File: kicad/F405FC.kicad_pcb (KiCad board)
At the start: 4 copper layers, 36 x 36 mm, 154 parts, among them J1 USB4105-GF-A, J2 ESC, J3 HD VTX, J4 GPS, J5 ELRS, P1 VBAT, P10 LED_DIN, P11 5V, P13 5V, P14 BUZ_N, P15 UART5_TX, P16 UART5_RX, P17 UART6_TX, P18 UART6_RX, P19 MOTOR5, P2 GND, P20 MOTOR6, P21 MOTOR7, P22 MOTOR8, P23 RSSI_IN, P24 GND, P25 5V, P3 10V, P4 GND, P5 CAM1_VID, P6 CAM2_VID, P7 VTX_VID, P8 5V, P9 GND, Q1 PMV40UN2, Q2 NX7002AK, SW1 BOOT, U1 LMR38020FSDDAR, U10 W25N01GV, U11 TS5A3159A, U12 SN74LV1T125, U13 USBLC6-2SC6, U2 LMR38020FSDDAR, U3 STM32F405RGT6, U4 LP38692MP-3.3, U5 LP5907MFX-3.3, U6 ICM-42688-P, U7 BMI270, U8 BMP390, U9 IIS2MDC, Y1 8MHz

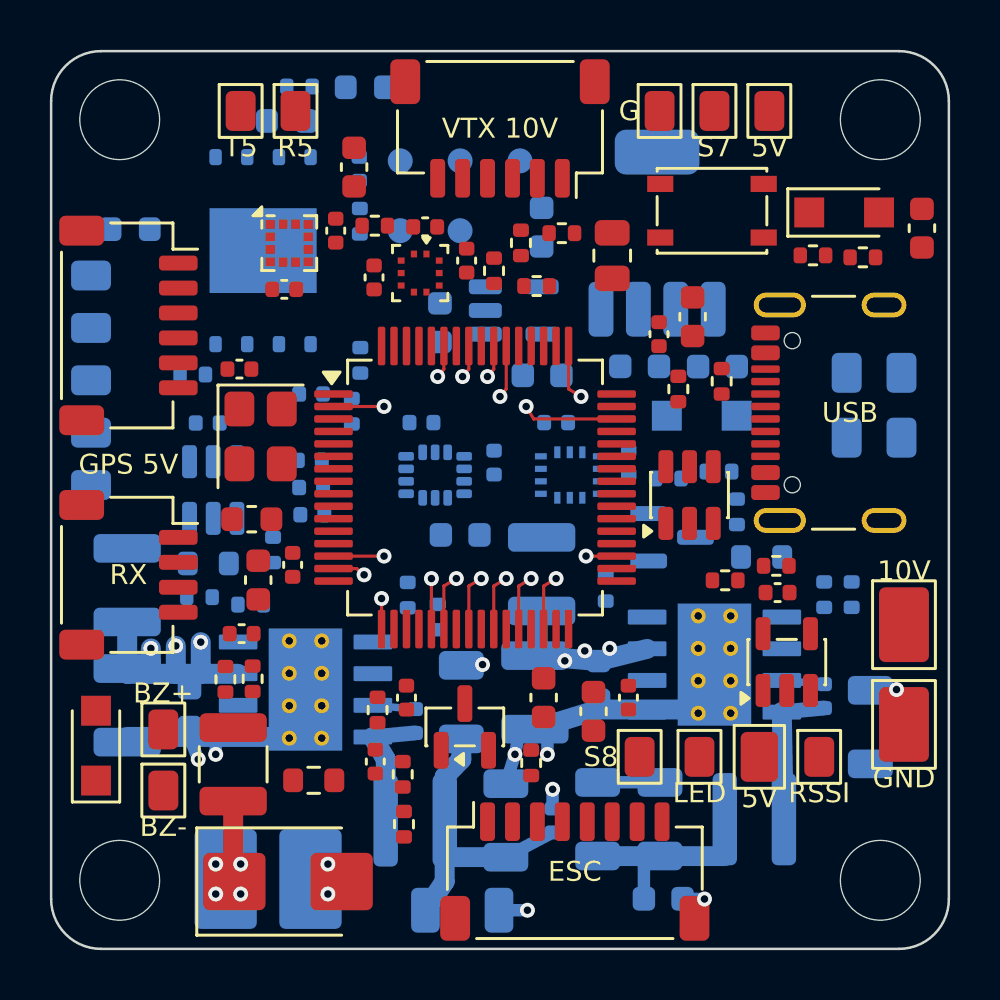
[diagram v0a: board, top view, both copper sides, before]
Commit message: Freerouting finishing step (gen/fr_finish.sh, route.py lockall stage)
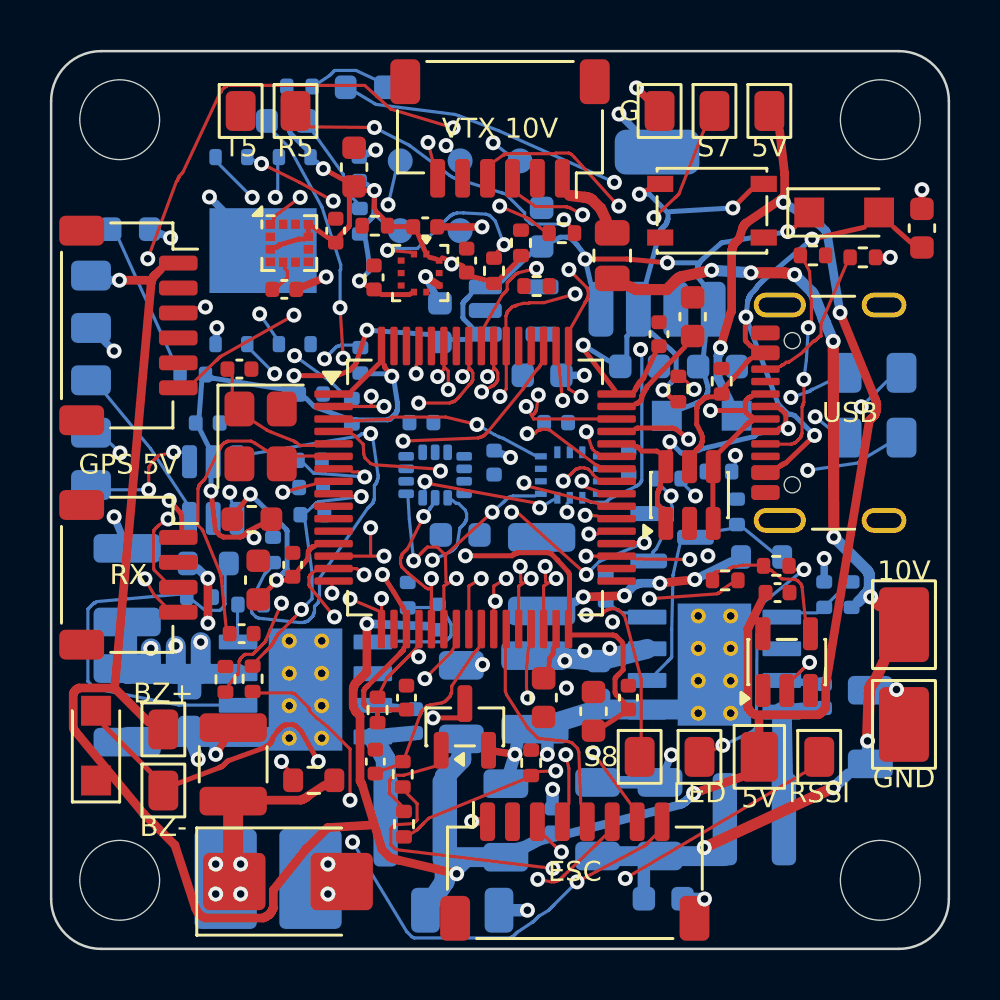
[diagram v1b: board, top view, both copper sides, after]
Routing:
- net 5V: track 10.5 -> 121.7 mm, vias 0 -> 7
- net 3V3: track 0.00 -> 90.8 mm, vias 0 -> 13
- net NRST: track 0.00 -> 38.0 mm, vias 0 -> 4
- net 5V_SYS: track 0.00 -> 33.7 mm, vias 0 -> 6
- net 10V: track 6.81 -> 38.8 mm, vias 0 -> 9
- net STATUS_LED_BLUE: track 1.22 -> 32.3 mm, vias 1 -> 3
- net GND: track 24.6 -> 53.4 mm, vias 11 -> 28
- net ESC_TLM: track 1.32 -> 29.3 mm, vias 1 -> 4
- net I2C1_SCL: track 0.00 -> 27.1 mm, vias 0 -> 5
- net VTX_PWR_EN: track 0.00 -> 26.2 mm, vias 0 -> 3
- net STATUS_LED_GREEN: track 0.00 -> 26.0 mm, vias 0 -> 5
- net SPI3_MISO: track 0.00 -> 23.2 mm, vias 0 -> 2
- net RSSI_IN: track 0.00 -> 21.0 mm, vias 0 -> 2
- net VBUS: track 0.00 -> 20.4 mm, vias 0 -> 3
- net CAM_SEL: track 2.03 -> 21.7 mm, vias 1 -> 3
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
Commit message: Freerouting finish in progress: base route set from PathFinder (6 conflicting nets dropped)
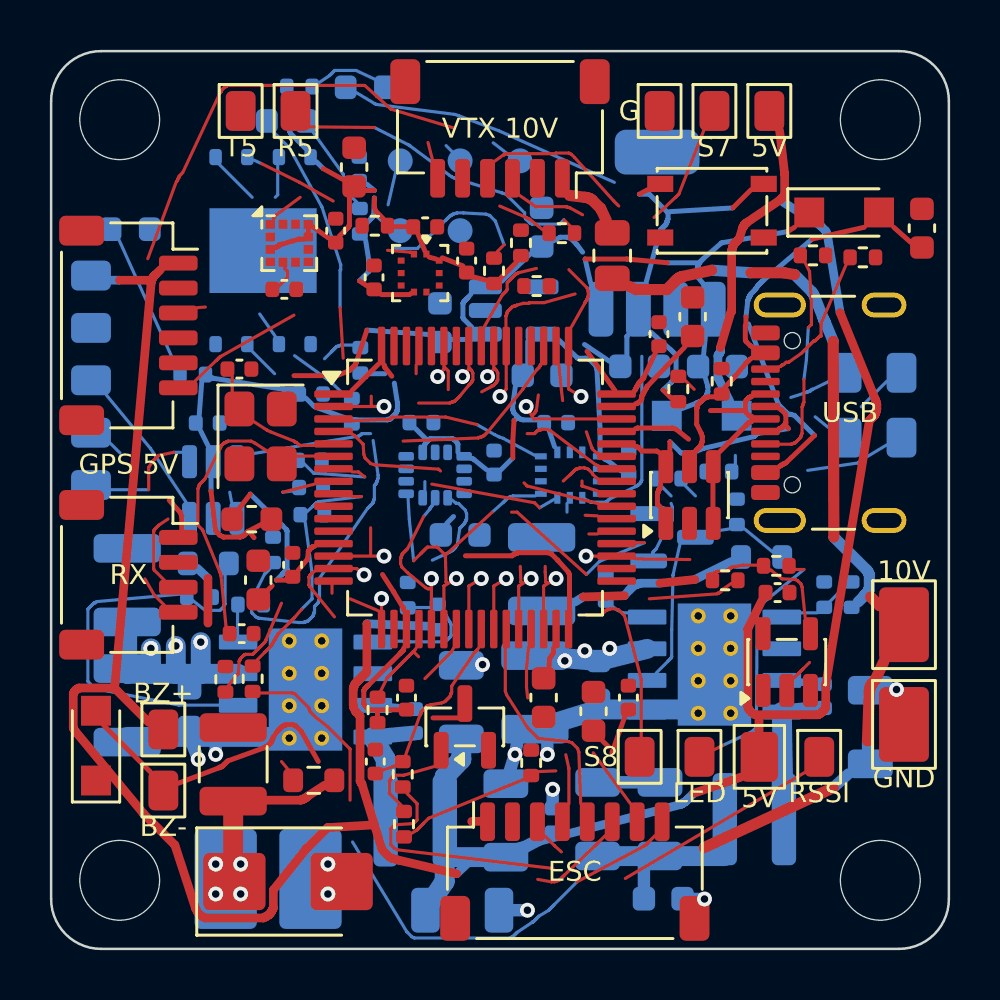
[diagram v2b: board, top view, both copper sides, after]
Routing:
- net GND: track 53.4 -> 24.6 mm, vias 28 -> 11
- net 3V3_IMU: track 0.00 -> 19.0 mm
- net 3V3: track 90.8 -> 102.0 mm, vias 13 -> 0
- net 5V: vias 7 -> 0
- net VTX_PWR_EN: vias 3 -> 0
- net NRST: vias 4 -> 0
- net I2C1_SCL: vias 5 -> 0
- net GYRO2_CS: vias 3 -> 0
- net CAM_SEL: vias 3 -> 1
- net 5V_SYS: vias 6 -> 0
- net 10V: vias 9 -> 0
- net VBAT: vias 17 -> 10
- net UART6_TX: vias 3 -> 0
- net UART6_RX: vias 2 -> 0
- net STATUS_LED_GREEN: vias 5 -> 0
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- removed copper zone on In1.Cu, net GND
- removed copper zone on In2.Cu, net VBAT

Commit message: Board checkpoint during Freerouting finish
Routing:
- net GND: track 24.6 -> 52.8 mm, vias 11 -> 26
- net VTX_VID: vias 0 -> 2
- net VTX_PWR_EN: vias 0 -> 3
- net VTX_OFF_G: vias 0 -> 2
- net VBUS: vias 0 -> 3
- net VBAT_ADC: vias 0 -> 3
- net VBAT: vias 10 -> 17
- net USB_DP: vias 0 -> 2
- net USB_DM: vias 0 -> 2
- net USB_CC1: vias 0 -> 2
- net UART6_TX: vias 0 -> 3
- net UART6_RX: vias 0 -> 2
- net UART5_RX: vias 1 -> 4
- net UART3_TX: vias 0 -> 2
- net UART2_TX: vias 0 -> 2
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- added copper zone on In1.Cu, net GND
- added copper zone on In2.Cu, net VBAT

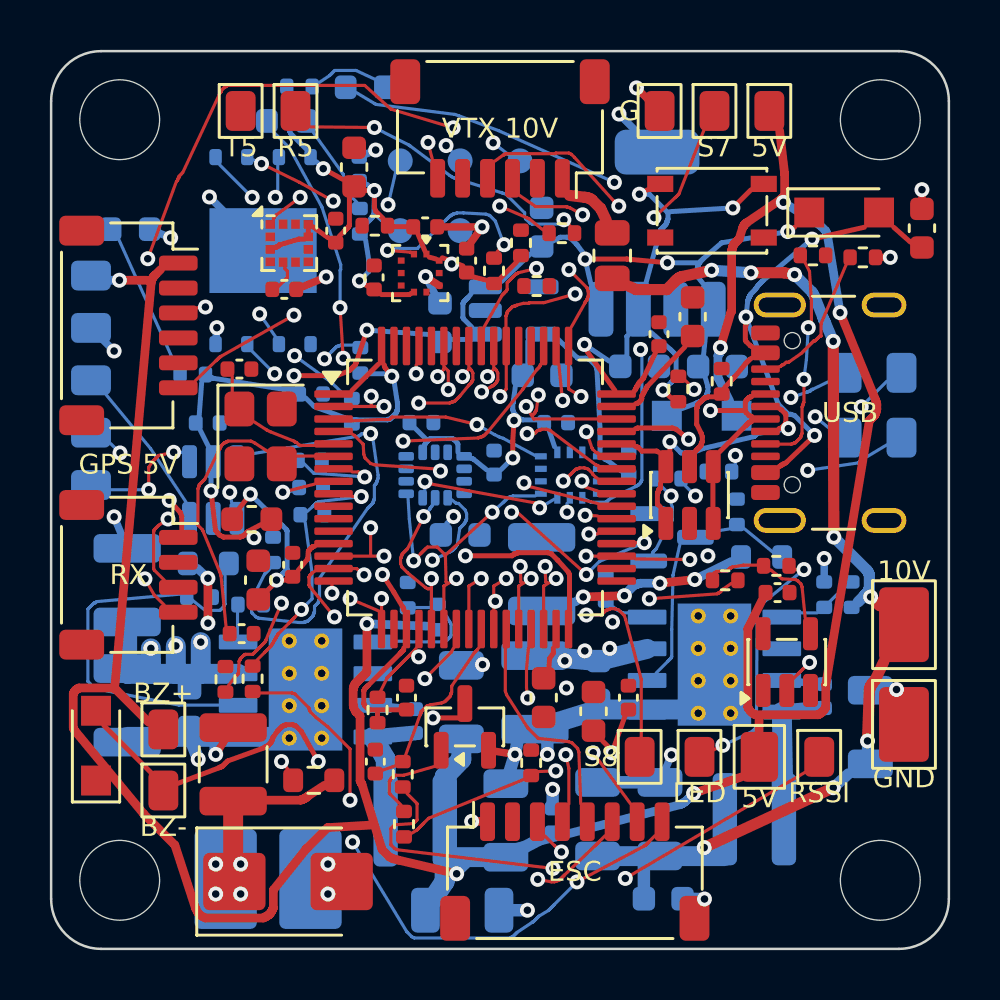
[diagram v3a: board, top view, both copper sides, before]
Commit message: Placement: I2C pull-ups R25/R26 moved west next to the sensors (routing); rexport includes NPTH holes; Freerouting finish attempt failed (documented)
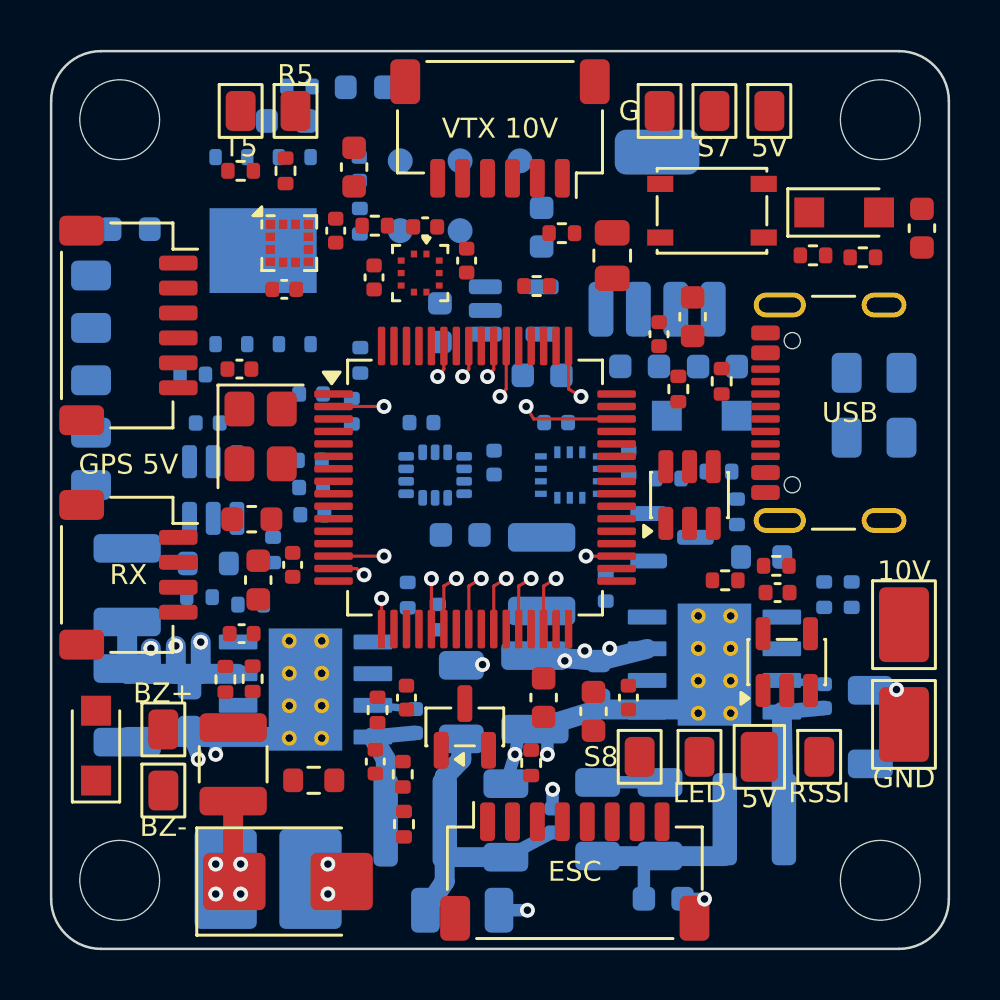
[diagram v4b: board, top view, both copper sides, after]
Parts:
- moved R25 10.9 mm to (107.6, 104.8), turned to 0 degrees
- moved R26 9.87 mm to (109.4, 104.8)
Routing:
- net 5V: track 121.7 -> 10.5 mm, vias 7 -> 0
- net 3V3: track 102.0 -> 0.00 mm, vias 14 -> 0
- net NRST: track 38.0 -> 0.00 mm, vias 4 -> 0
- net 5V_SYS: track 33.7 -> 0.00 mm, vias 6 -> 0
- net 10V: track 38.8 -> 6.81 mm, vias 9 -> 0
- net STATUS_LED_BLUE: track 32.3 -> 1.22 mm, vias 3 -> 1
- net GND: track 52.8 -> 24.6 mm, vias 26 -> 11
- net ESC_TLM: track 29.3 -> 1.32 mm, vias 4 -> 1
- net I2C1_SCL: track 27.1 -> 0.00 mm, vias 5 -> 0
- net VTX_PWR_EN: track 26.2 -> 0.00 mm, vias 3 -> 0
- net STATUS_LED_GREEN: track 26.0 -> 0.00 mm, vias 5 -> 0
- net SPI3_MISO: track 23.2 -> 0.00 mm, vias 2 -> 0
- net RSSI_IN: track 21.0 -> 0.00 mm, vias 2 -> 0
- net VBUS: track 20.4 -> 0.00 mm, vias 3 -> 0
- net CAM_SEL: track 21.7 -> 2.03 mm, vias 3 -> 1
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
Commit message: Converged signal routing (alt15) checkpoint; router hole clearance margin; solid pour connections on all pads
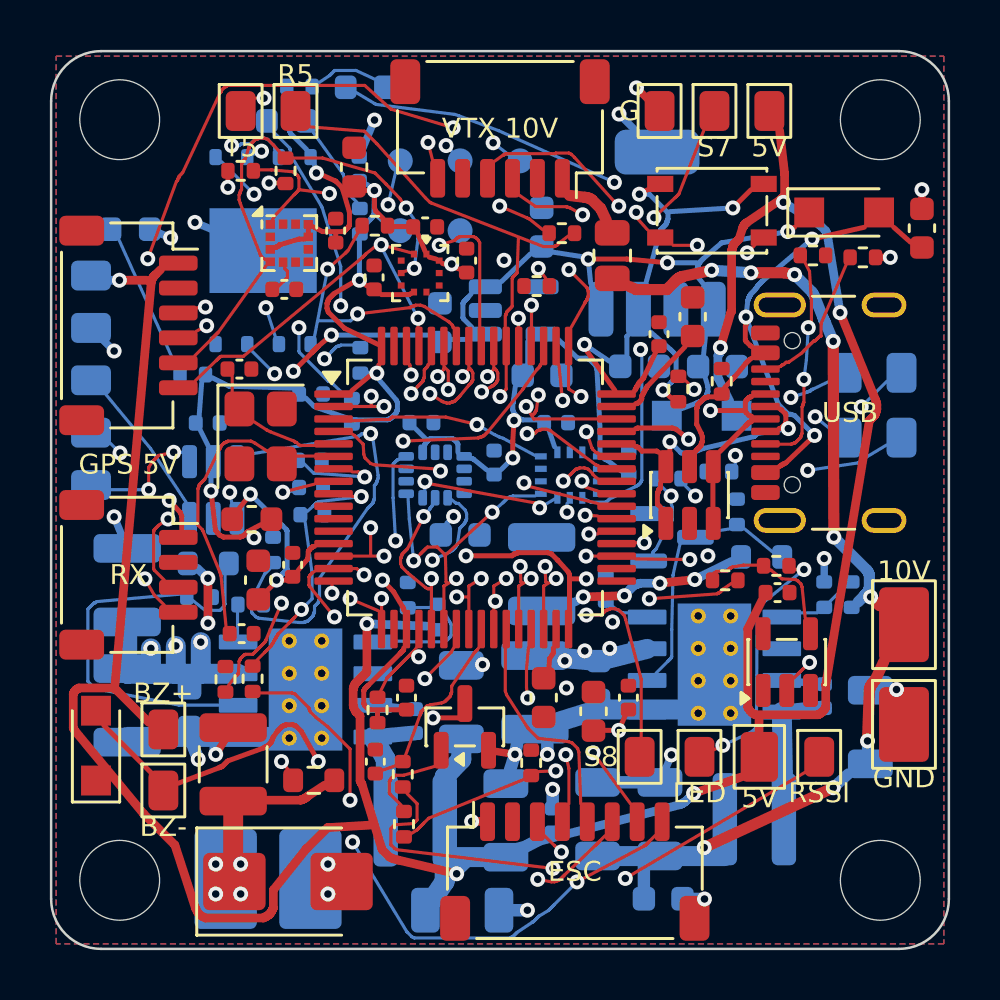
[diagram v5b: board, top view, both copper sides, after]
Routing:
- net 5V: track 10.5 -> 121.7 mm, vias 0 -> 7
- net 3V3: track 0.00 -> 96.9 mm, vias 0 -> 17
- net NRST: track 0.00 -> 38.0 mm, vias 0 -> 4
- net 5V_SYS: track 0.00 -> 32.7 mm, vias 0 -> 6
- net 10V: track 6.81 -> 38.8 mm, vias 0 -> 9
- net STATUS_LED_BLUE: track 1.22 -> 32.3 mm, vias 1 -> 3
- net ESC_TLM: track 1.32 -> 29.3 mm, vias 1 -> 4
- net STATUS_LED_GREEN: track 0.00 -> 26.6 mm, vias 0 -> 2
- net VTX_PWR_EN: track 0.00 -> 26.2 mm, vias 0 -> 3
- net I2C1_SDA: track 0.00 -> 24.0 mm, vias 0 -> 3
- net GND: track 24.6 -> 46.9 mm, vias 11 -> 22
- net I2C1_SCL: track 0.00 -> 21.7 mm, vias 0 -> 3
- net RSSI_IN: track 0.00 -> 21.0 mm, vias 0 -> 2
- net VBUS: track 0.00 -> 20.4 mm, vias 0 -> 3
- net BOOT0: track 0.00 -> 20.2 mm, vias 0 -> 5
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- added copper zone on B.Cu, net GND
- added copper zone on F.Cu, net GND
- added copper zone on In2.Cu, net GND

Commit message: Router: all GND ties renegotiable; gnd_need recomputed on the converged signal routing (32 fragments)
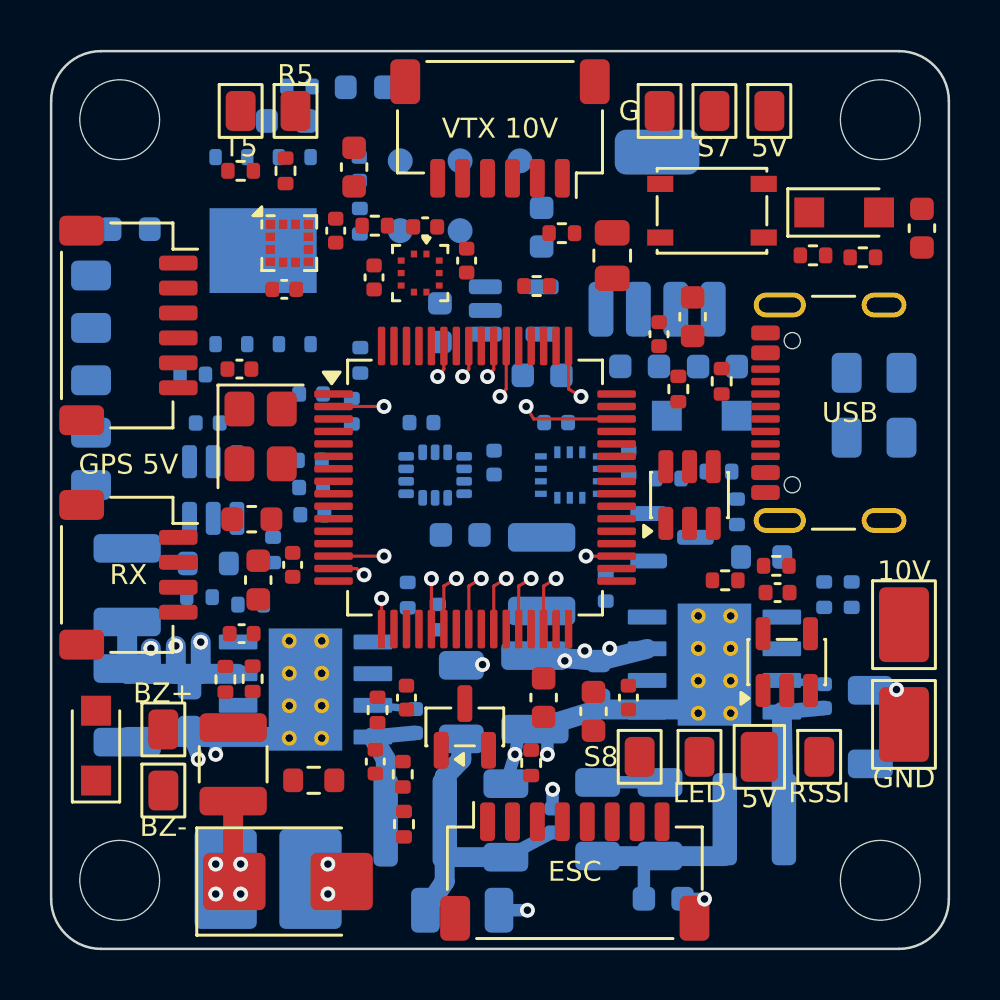
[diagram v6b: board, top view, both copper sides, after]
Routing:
- net 5V: track 121.7 -> 10.5 mm, vias 7 -> 0
- net 3V3: track 96.9 -> 0.00 mm, vias 17 -> 0
- net NRST: track 38.0 -> 0.00 mm, vias 4 -> 0
- net 5V_SYS: track 32.7 -> 0.00 mm, vias 6 -> 0
- net 10V: track 38.8 -> 6.81 mm, vias 9 -> 0
- net STATUS_LED_BLUE: track 32.3 -> 1.22 mm, vias 3 -> 1
- net ESC_TLM: track 29.3 -> 1.32 mm, vias 4 -> 1
- net STATUS_LED_GREEN: track 26.6 -> 0.00 mm, vias 2 -> 0
- net VTX_PWR_EN: track 26.2 -> 0.00 mm, vias 3 -> 0
- net I2C1_SDA: track 24.0 -> 0.00 mm, vias 3 -> 0
- net GND: track 46.9 -> 24.6 mm, vias 22 -> 11
- net I2C1_SCL: track 21.7 -> 0.00 mm, vias 3 -> 0
- net RSSI_IN: track 21.0 -> 0.00 mm, vias 2 -> 0
- net VBUS: track 20.4 -> 0.00 mm, vias 3 -> 0
- net BOOT0: track 20.2 -> 0.00 mm, vias 5 -> 0
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- removed copper zone on B.Cu, net GND
- removed copper zone on F.Cu, net GND
- removed copper zone on In2.Cu, net GND

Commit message: Routing nearly closed: finisher (gen/pffinish.py) on best negotiation state, 3V3_IMU/3V3A to Default class (<=10 mA). DRC: 2 clearance (5 um), 3 GND islands, parity 0
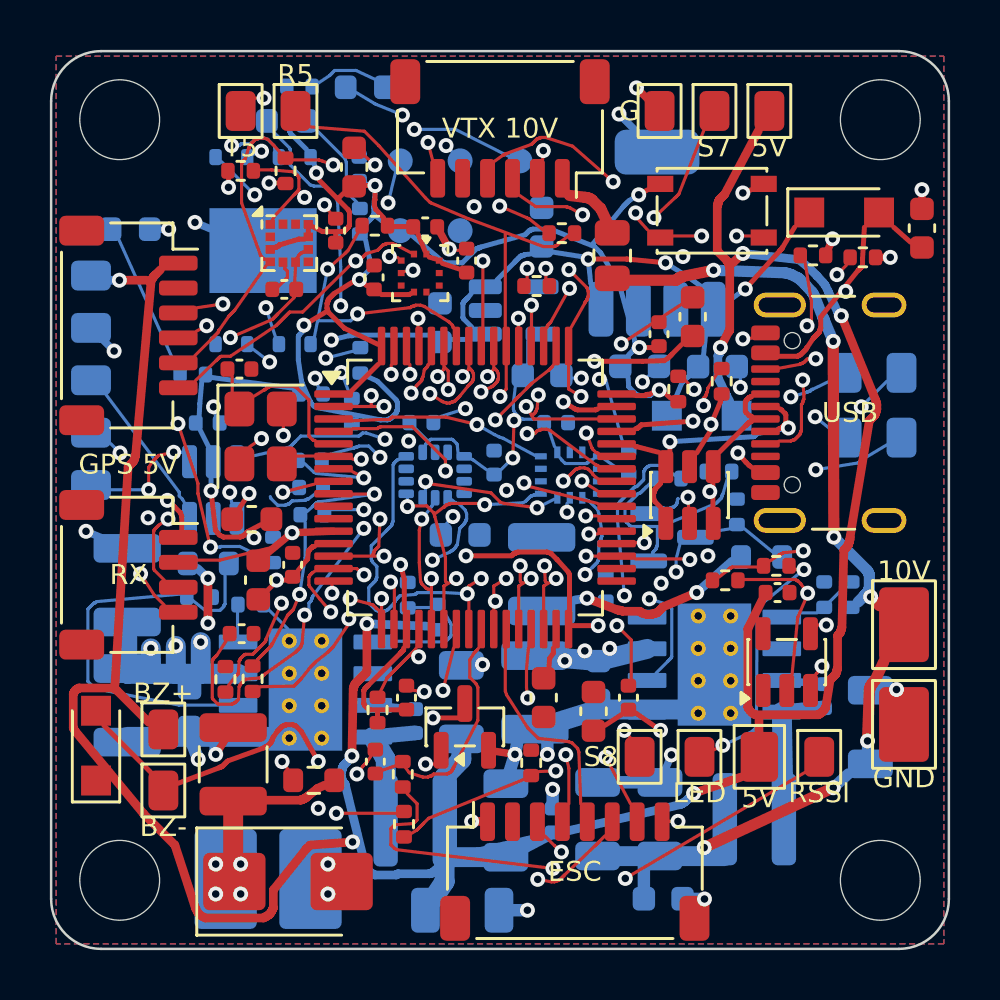
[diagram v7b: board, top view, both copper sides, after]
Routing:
- net 5V: track 10.5 -> 122.3 mm, vias 0 -> 8
- net 3V3: track 0.00 -> 102.7 mm, vias 0 -> 16
- net GND: track 24.6 -> 86.5 mm, vias 11 -> 50
- net 10V: track 6.81 -> 38.6 mm, vias 0 -> 7
- net 5V_SYS: track 0.00 -> 31.6 mm, vias 0 -> 5
- net NRST: track 0.00 -> 31.6 mm, vias 0 -> 2
- net STATUS_LED_BLUE: track 1.22 -> 30.8 mm, vias 1 -> 4
- net STATUS_LED_GREEN: track 0.00 -> 26.3 mm, vias 0 -> 3
- net ESC_CURR: track 0.00 -> 23.8 mm, vias 0 -> 3
- net CAM_SEL: track 2.03 -> 25.6 mm, vias 1 -> 5
- net GYRO2_CS: track 0.00 -> 22.8 mm, vias 0 -> 4
- net I2C1_SDA: track 0.00 -> 22.8 mm, vias 0 -> 3
- net VTX_PWR_EN: track 0.00 -> 21.8 mm, vias 0 -> 2
- net I2C1_SCL: track 0.00 -> 21.4 mm, vias 0 -> 3
- net RSSI_IN: track 0.00 -> 21.0 mm, vias 0 -> 2
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- added copper zone on B.Cu, net GND
- added copper zone on F.Cu, net GND
- added copper zone on In2.Cu, net GND
